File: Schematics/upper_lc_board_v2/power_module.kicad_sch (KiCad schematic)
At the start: 37 parts, among them J2 Stack Male Edge Connector, Q5 2N7002, U3 AMS1117, U4 ID_LM66100DCKR, U5 ID_LM66100DCKR, U9 DMP4065S-7

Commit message: layout updates after review, cleaned up schematic organization
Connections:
- net +24V_BP: now also J2.A17 (24V_A); no longer J2.A16 (24V_A)
- net GND: no longer J2.A12 (GND_B), J2.A9 (GND_B), J2.B10 (GND_B), J2.B11 (GND_B), J2.B12 (GND_B)
- new net: J2.A12 (GND_B), J2.A9 (GND_B), J2.B10 (GND_B), J2.B11 (GND_B), J2.B12 (GND_B)
- no-connect marks 4 -> 5
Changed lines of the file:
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@@
 	)
 	(junction
-		(at 80.01 43.18)
-		(diameter 0)
-		(color 0 0 0 0)
-	)
-	(junction
 		(at 179.07 66.04)
 		(diameter 0)
@@
 		(color 0 0 0 0)
 	)
+	(junction
+		(at 80.01 43.18)
+		(diameter 0)
+		(color 0 0 0 0)
+	)
 	(no_connect
 		(at 52.07 43.18)
 	)
 	(no_connect
+		(at 80.01 80.01)
+	)
+	(no_connect
 		(at 80.01 76.2)
 	)
@@
 	)
 	(symbol
-		(lib_id "power:GND")
-		(at 80.01 80.01 90)
-		(unit 1)
-		(exclude_from_sim no)
-		(in_bom yes)
-		(on_board yes)
-		(dnp no)
-		(fields_autoplaced yes)
-		(property "Reference" "#PWR029"
-			(at 86.36 80.01 0)
-			(effects
-				(font
-					(size 1.27 1.27)
-				)
-				(hide yes)
-			)
-		)
-		(property "Value" "GND"
-			(at 83.82 80.0099 90)
-			(effects
-				(font
-					(size 1.27 1.27)
-				)
-				(justify right)
-			)
-		)
-		(property "Footprint" ""
-			(at 80.01 80.01 0)
-			(effects
-				(font
-					(size 1.27 1.27)
-				)
-				(hide yes)
-			)
-		)
-		(property "Datasheet" ""
-			(at 80.01 80.01 0)
-			(effects
-				(font
-					(size 1.27 1.27)
-				)
-				(hide yes)
-			)
-		)
-		(property "Description" "Power symbol creates a global label with name \"GND\" , ground"
-			(at 80.01 80.01 0)
-			(effects
-				(font
-					(size 1.27 1.27)
-				)
-				(hide yes)
-			)
-		)
-		(pin "1"
-		)
-		(instances
-			(project "upper_lc_board_v2"
-				(path "/8de962ac-ee95-4233-a205-efbcd04063bc/94566a7d-86bb-4a04-89fe-f21a893d6a23"
-					(reference "#PWR029")
-					(unit 1)
-				)
-			)
-		)
-	)
-	(symbol
 		(lib_id "Device:R")
 		(at 228.6 45.72 270)
@@
 	)
 	(symbol
-		(lib_id "EdgeConnectorV2:Stack Male Edge Connector")
-		(at 66.04 62.23 0)
-		(unit 1)
-		(exclude_from_sim no)
-		(in_bom yes)
-		(on_board yes)
-		(dnp no)
-		(fields_autoplaced yes)
-		(property "Reference" "J2"
-			(at 66.04 35.56 0)
-			(effects
-				(font
-					(size 1.27 1.27)
-				)
-			)
-		)
-		(property "Value" "Stack Male Edge Connector"
-			(at 66.04 38.1 0)
-			(effects
-				(font
-					(size 1.27 1.27)
-				)
-			)
-		)
-		(property "Footprint" "Connector_PCBEdge:BUS_PCIexpress_x1"
-			(at 66.04 85.09 0)
-			(effects
-				(font
-					(size 1.27 1.27)
-				)
-				(hide yes)
-			)
-		)
-		(property "Datasheet" ""
-			(at 60.706 81.28 0)
-			(effects
-				(font
-					(size 1.27 1.27)
-				)
-				(hide yes)
-			)
-		)
-		(property "Description" "QRET SRAD Male Stack Edge Connector (PCIe x1 Connector). Generation 2"
-			(at 62.23 57.912 0)
-			(effects
-				(font
-					(size 1.27 1.27)
-				)
-				(hide yes)
-			)
-		)
-		(pin "B3"
-		)
-		(pin "A10"
-		)
-		(pin "A3"
-		)
-		(pin "B4"
-		)
-		(pin "B10"
-		)
-		(pin "A17"
-		)
-		(pin "B13"
-		)
-		(pin "A1"
-		)
-		(pin "A11"
-		)
-		(pin "A14"
-		)
-		(pin "A15"
-		)
-		(pin "A7"
-		)
-		(pin "B12"
-		)
-		(pin "B16"
-		)
-		(pin "B14"
-		)
-		(pin "A13"
-		)
-		(pin "A16"
-		)
-		(pin "B11"
-		)
-		(pin "A18"
-		)
-		(pin "A2"
-		)
-		(pin "B15"
-		)
-		(pin "B1"
-		)
-		(pin "A6"
-		)
-		(pin "B17"
-		)
-		(pin "B18"
-		)
-		(pin "B5"
-		)
-		(pin "A9"
-		)
-		(pin "B6"
-		)
-		(pin "A5"
-		)
-		(pin "B2"
-		)
-		(pin "A4"
-		)
-		(pin "B7"
-		)
-		(pin "B8"
-		)
-		(pin "B9"
-		)
-		(pin "A8"
-		)
-		(pin "A12"
-		)
-		(instances
-			(project "upper_lc_board_v2"
-				(path "/8de962ac-ee95-4233-a205-efbcd04063bc/94566a7d-86bb-4a04-89fe-f21a893d6a23"
-					(reference "J2")
-					(unit 1)
-				)
-			)
-		)
-	)
-	(symbol
 		(lib_id "QRET_Buck_PSU:LM66100DCKR")
 		(at 151.13 53.34 0)
@@
 					(unit 1)
 				)
+			)
+		)
+	)
+	(symbol
+		(lib_id "EdgeConnectorV2:Stack Male Edge Connector")
+		(at 66.04 62.23 0)
+		(unit 1)
+		(exclude_from_sim no)
+		(in_bom yes)
+		(on_board yes)
+		(dnp no)
+		(fields_autoplaced yes)
+		(property "Reference" "J2"
+			(at 66.04 35.56 0)
+			(effects
+				(font
+					(size 1.27 1.27)
+				)
+			)
+		)
+		(property "Value" "Stack Male Edge Connector"
+			(at 66.04 38.1 0)
+			(effects
+				(font
+					(size 1.27 1.27)
+				)
+			)
+		)
+		(property "Footprint" "Connector_PCBEdge:BUS_PCIexpress_x1"
+			(at 66.04 85.09 0)
+			(effects
+				(font
+					(size 1.27 1.27)
+				)
+				(hide yes)
+			)
+		)
+		(property "Datasheet" ""
+			(at 60.706 81.28 0)
+			(effects
+				(font
+					(size 1.27 1.27)
+				)
+				(hide yes)
+			)
+		)
+		(property "Description" "QRET SRAD Male Stack Edge Connector (PCIe x1 Connector). Generation 2"
+			(at 62.23 57.912 0)
+			(effects
+				(font
+					(size 1.27 1.27)
+				)
+				(hide yes)
+			)
+		)
+		(pin "A13"
+		)
+		(pin "A7"
+		)
+		(pin "A11"
+		)
+		(pin "A15"
+		)
+		(pin "A16"
+		)
+		(pin "A2"
+		)
+		(pin "A4"
+		)
+		(pin "A12"
+		)
+		(pin "A14"
+		)
+		(pin "A1"
+		)
+		(pin "A17"
+		)
+		(pin "A10"
+		)
+		(pin "A5"
+		)
+		(pin "A6"
+		)
+		(pin "A3"
+		)
+		(pin "A18"
+		)
+		(pin "A8"
+		)
+		(pin "A9"
+		)
+		(pin "B10"
+		)
+		(pin "B11"
+		)
+		(pin "B13"
+		)
+		(pin "B12"
+		)
+		(pin "B14"
+		)
+		(pin "B16"
+		)
+		(pin "B17"
+		)
+		(pin "B15"
+		)
+		(pin "B18"
+		)
+		(pin "B1"
+		)
+		(pin "B2"
+		)
+		(pin "B7"
+		)
+		(pin "B9"
+		)
+		(pin "B3"
+		)
+		(pin "B5"
+		)
+		(pin "B4"
+		)
+		(pin "B8"
+		)
+		(pin "B6"
+		)
+		(instances
+			(project ""
+				(path "/8de962ac-ee95-4233-a205-efbcd04063bc/94566a7d-86bb-4a04-89fe-f21a893d6a23"
+					(reference "J2")
+					(unit 1)
+				)

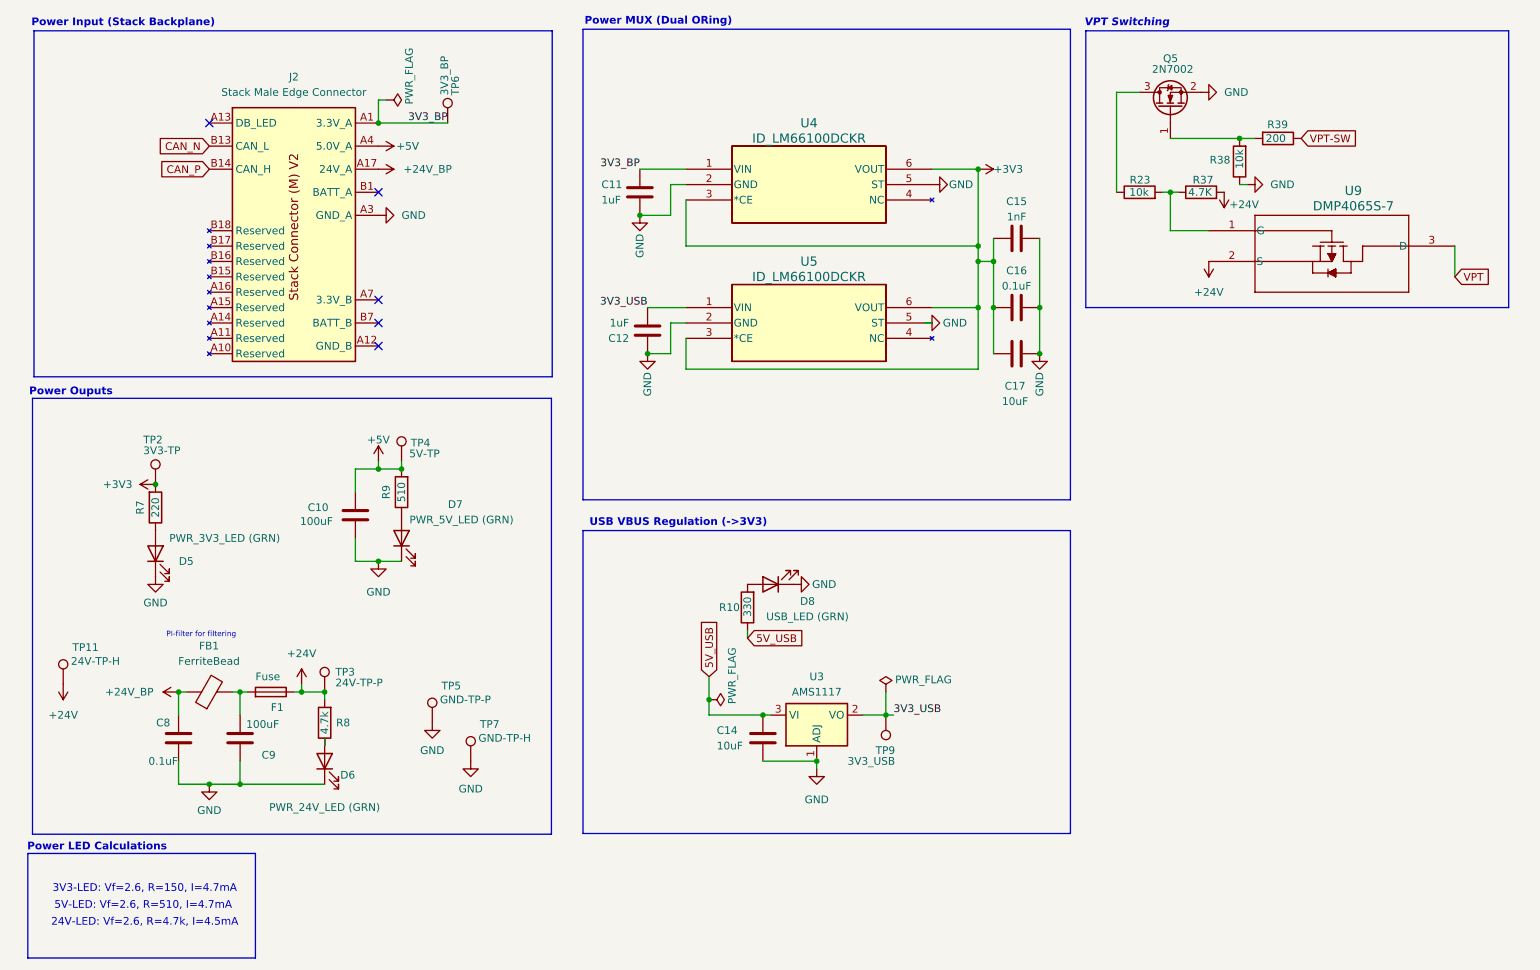
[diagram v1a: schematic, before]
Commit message: updated part numbers and fixed minor circuit issues
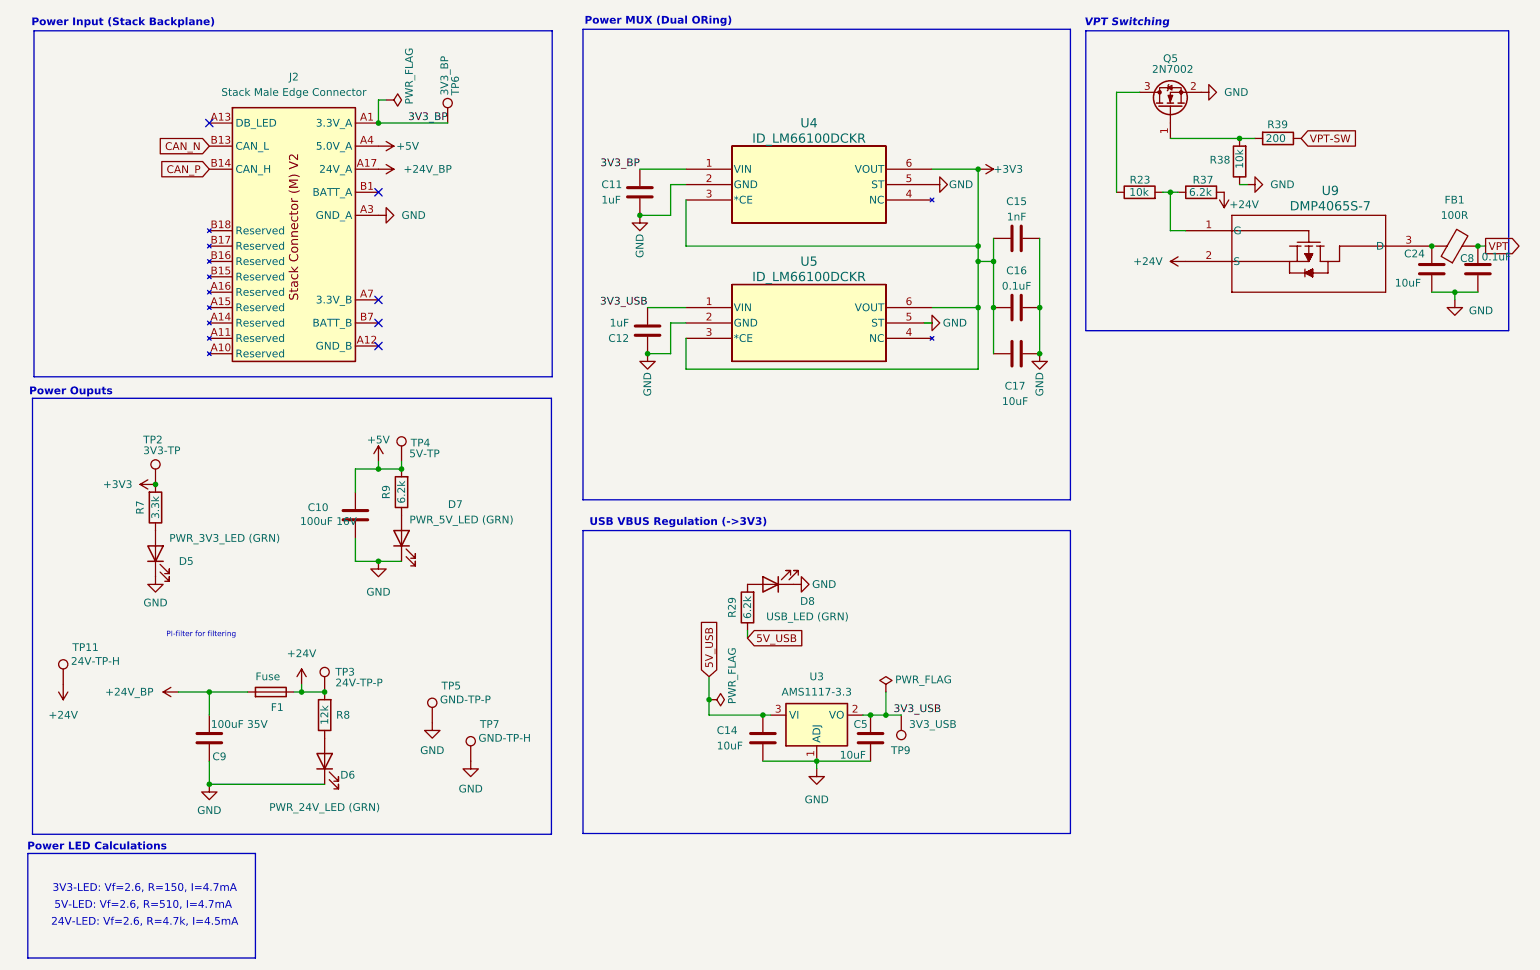
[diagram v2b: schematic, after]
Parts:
- removed R10: 330, Resistor_SMD:R_0603_1608Metric, symbol Device:R
- added C24: 10uF, Capacitor_SMD:C_1206_3216Metric, symbol Device:C
- added C5: 10uF, Capacitor_SMD:C_0603_1608Metric, symbol Device:C
- added R29: 6.2k, Resistor_SMD:R_0603_1608Metric, symbol Device:R
- C10: value 100uF -> 100uF 16V
- C11, C12: JLCPCB C15849 -> (none)
- C14: JLCPCB C96446 -> (none)
- C15: JLCPCB C1588 -> (none); LCSC (none) -> C1588
- C16: JLCPCB C14663 -> (none); LCSC (none) -> C14663
- C17: JLCPCB C96446 -> (none); LCSC (none) -> C96446
- C8: JLCPCB C14663 -> (none)
- C9: value 100uF -> 100uF 35V
- FB1: value FerriteBead -> 100R; LCSC (none) -> C1015
- Q5: JLCPCB C8545 -> (none); LCSC (none) -> C8545
- R23: JLCPCB C25804 -> (none); LCSC (none) -> C25804
- R37: value 4.7K -> 6.2k; footprint Resistor_SMD:R_0805_2012Metric -> Resistor_SMD:R_0603_1608Metric; JLCPCB C23162 -> (none); LCSC (none) -> C4260
- R38: LCSC (none) -> C25804
- R39: LCSC (none) -> C8218
- R7: value 220 -> 3.3k; LCSC C22808 -> C22978
- R8: value 4.7k -> 12k; Digikey 311-4.70KFRCT-ND -> 311-12.1KFRCT-ND; JLCPCB C17936 -> (none); LCSC (none) -> C17912
- R9: value 510 -> 6.2k; LCSC C23193 -> C4260
- U3: value AMS1117 -> AMS1117-3.3; LCSC (none) -> C6186
- U9: LCSC (none) -> C182476
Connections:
- net +24V_BP: now also C9.1, F1.2; no longer C8.1, FB1.1
- net 3V3_USB: now also C5.1
- net 5V_USB: now also R29.1
- net GND: now also C24.2, C5.2
- net VPT: now also C8.1, FB1.2; no longer U9.3 (D)
- net at D8.2 (A): now also R29.2
- new net: C24.1, FB1.1, U9.3 (D)
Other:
- moved on the sheet: C9, R8, TP9, U9

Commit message: updated silkscree and changed PI caps
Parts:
- C24: value 10uF -> 0.1uF; footprint Capacitor_SMD:C_1206_3216Metric -> Capacitor_SMD:C_0603_1608Metric; LCSC C13585 -> C14663
- C8: value 0.1uF -> 10uF; LCSC C14663 -> C96446
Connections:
- net VPT: now also C24.1; no longer C8.1
- net at FB1.1, U9.3 (D): now also C8.1; no longer C24.1
